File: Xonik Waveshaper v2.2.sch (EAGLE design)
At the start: 77 parts, among them IC1 TL074JT, IC2 TL074JT, IC3 TL074JT, IC4 TL072JT, IC5 4013T, IC6 LM311T, T1 2n3904

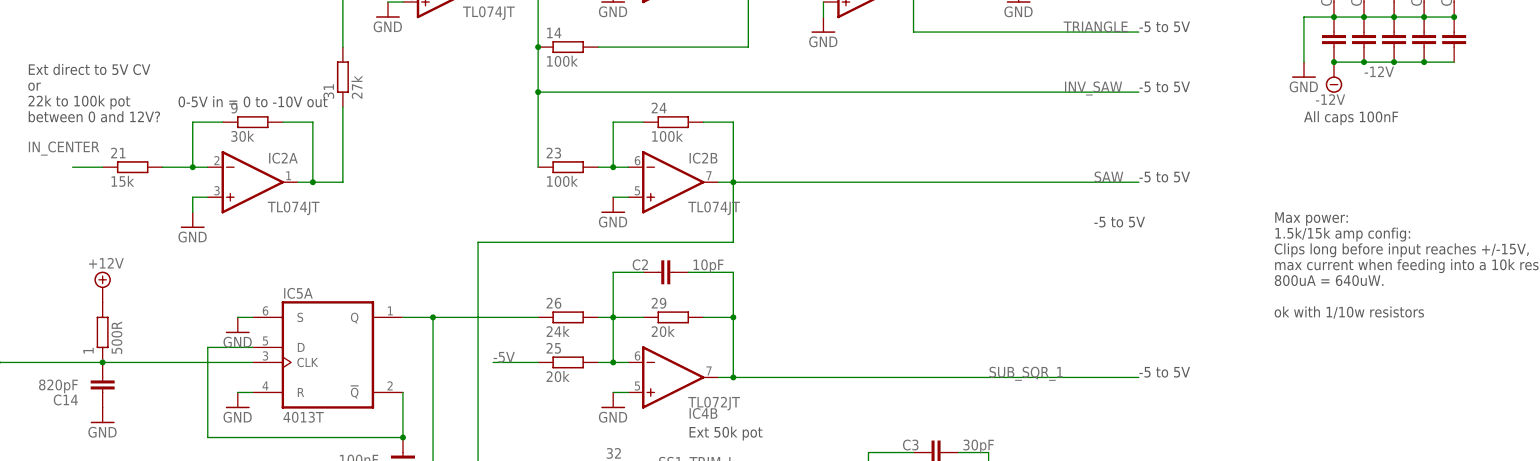
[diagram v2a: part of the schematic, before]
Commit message: Changed to standard value on waveshaper comparator pullup
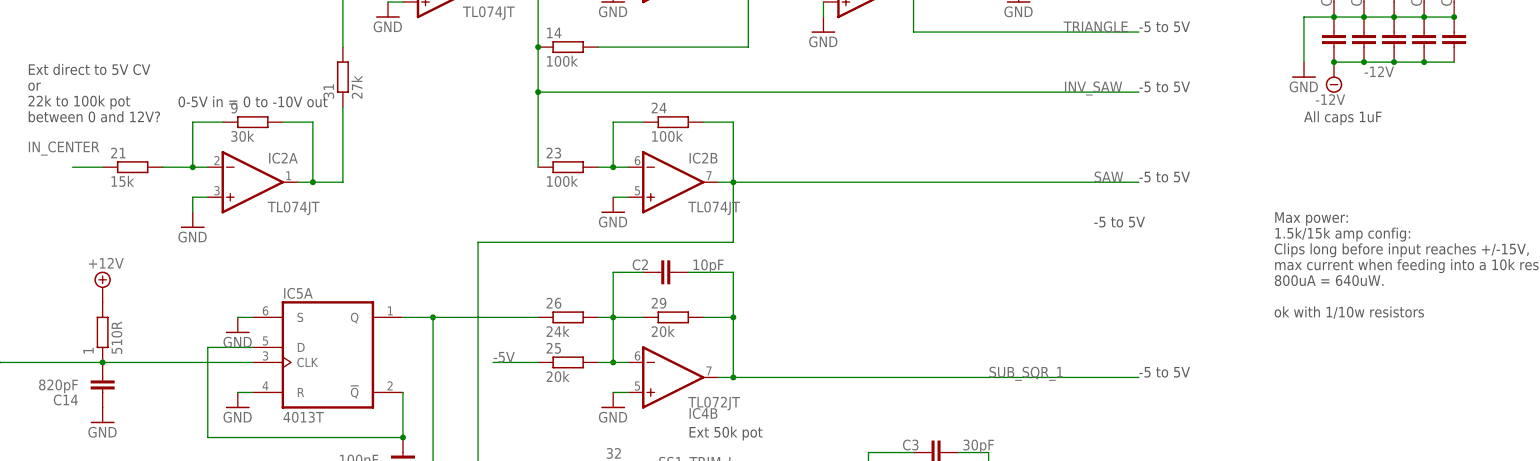
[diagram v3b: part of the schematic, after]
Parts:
- 1: value 500R -> 510R
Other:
- note added: "All caps 1uF"
- note removed: "All caps 100nF"
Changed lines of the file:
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@@
 <layer number="59" name="tCarbon" color="7" fill="1" visible="no" active="no"/>
 <layer number="60" name="bCarbon" color="7" fill="1" visible="no" active="no"/>
-<layer number="88" name="SimResults" color="9" fill="1" visible="yes" active="yes"/>
-<layer number="89" name="SimProbes" color="9" fill="1" visible="yes" active="yes"/>
-<layer number="90" name="Modules" color="5" fill="1" visible="yes" active="yes"/>
+<layer number="88" name="SimResults" color="9" fill="1" visible="no" active="yes"/>
+<layer number="89" name="SimProbes" color="9" fill="1" visible="no" active="yes"/>
+<layer number="90" name="Modules" color="5" fill="1" visible="no" active="yes"/>
 <layer number="91" name="Nets" color="2" fill="1" visible="yes" active="yes"/>
 <layer number="92" name="Busses" color="1" fill="1" visible="no" active="yes"/>
@@
 <layer number="127" name="Info2" color="7" fill="1" visible="no" active="yes"/>
 <layer number="128" name="_bValues" color="7" fill="1" visible="no" active="yes"/>
-<layer number="129" name="Mask" color="7" fill="1" visible="yes" active="yes"/>
+<layer number="129" name="Mask" color="7" fill="1" visible="no" active="yes"/>
 <layer number="130" name="SMDSTROOK" color="7" fill="1" visible="no" active="yes"/>
 <layer number="131" name="tAdjust" color="7" fill="1" visible="no" active="yes"/>
@@
 <layer number="223" name="223bmp" color="24" fill="1" visible="no" active="no"/>
 <layer number="224" name="224bmp" color="25" fill="1" visible="no" active="no"/>
-<layer number="225" name="225bmp" color="7" fill="1" visible="yes" active="yes"/>
-<layer number="226" name="226bmp" color="7" fill="1" visible="yes" active="yes"/>
-<layer number="227" name="227bmp" color="7" fill="1" visible="yes" active="yes"/>
-<layer number="228" name="228bmp" color="7" fill="1" visible="yes" active="yes"/>
-<layer number="229" name="229bmp" color="7" fill="1" visible="yes" active="yes"/>
-<layer number="230" name="230bmp" color="7" fill="1" visible="yes" active="yes"/>
+<layer number="225" name="225bmp" color="7" fill="1" visible="no" active="yes"/>
+<layer number="226" name="226bmp" color="7" fill="1" visible="no" active="yes"/>
+<layer number="227" name="227bmp" color="7" fill="1" visible="no" active="yes"/>
+<layer number="228" name="228bmp" color="7" fill="1" visible="no" active="yes"/>
+<layer number="229" name="229bmp" color="7" fill="1" visible="no" active="yes"/>
+<layer number="230" name="230bmp" color="7" fill="1" visible="no" active="yes"/>
 <layer number="231" name="Eagle3D_PG1" color="7" fill="1" visible="no" active="no"/>
 <layer number="232" name="Eagle3D_PG2" color="7" fill="1" visible="no" active="no"/>
@@
 <part name="C14" library="joakim" deviceset="C-EU-J" device="0603" value="820pF"/>
 <part name="GND9" library="supply1" library_urn="urn:adsk.eagle:library:371" deviceset="GND" device=""/>
-<part name="1" library="rcl" library_urn="urn:adsk.eagle:library:334" deviceset="R-EU_" device="R0603" package3d_urn="urn:adsk.eagle:package:23555/3" value="500R"/>
+<part name="1" library="rcl" library_urn="urn:adsk.eagle:library:334" deviceset="R-EU_" device="R0603" package3d_urn="urn:adsk.eagle:package:23555/3" value="510R"/>
 <part name="SUPPLY1" library="supply2" library_urn="urn:adsk.eagle:library:372" deviceset="+12V" device=""/>
 <part name="GND12" library="supply1" library_urn="urn:adsk.eagle:library:371" deviceset="GND" device=""/>
@@
 <sheet>
 <plain>
-<text x="129.54" y="22.86" size="1.778" layer="97">All caps 100nF</text>
+<text x="129.54" y="22.86" size="1.778" layer="97">All caps 1uF</text>
 <text x="-86.36" y="22.86" size="1.778" layer="97">Ext direct to 5V CV
 or
